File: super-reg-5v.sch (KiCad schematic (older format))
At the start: 41 parts, among them Q1 2SA1015, Q2 D44H11, U1 LM317T, U2 AD825, U3 AD825, X1 AC_IN, X2 DC_OUT

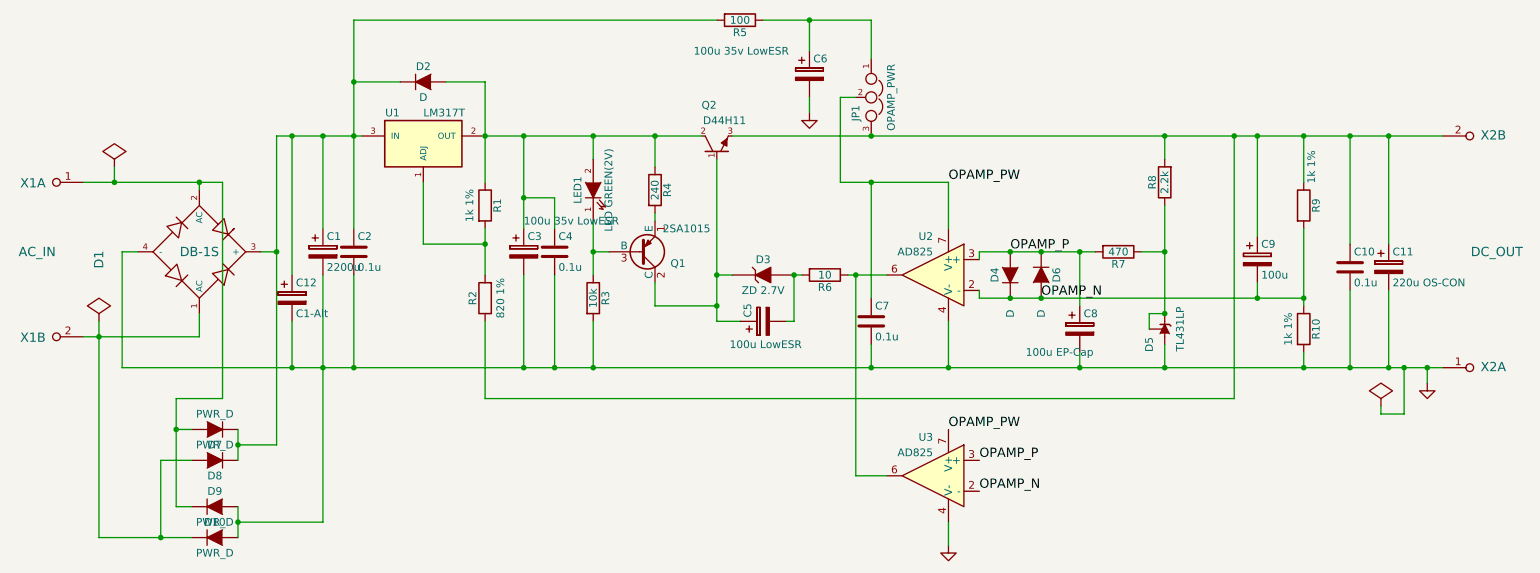
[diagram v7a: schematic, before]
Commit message: change bypass Cap
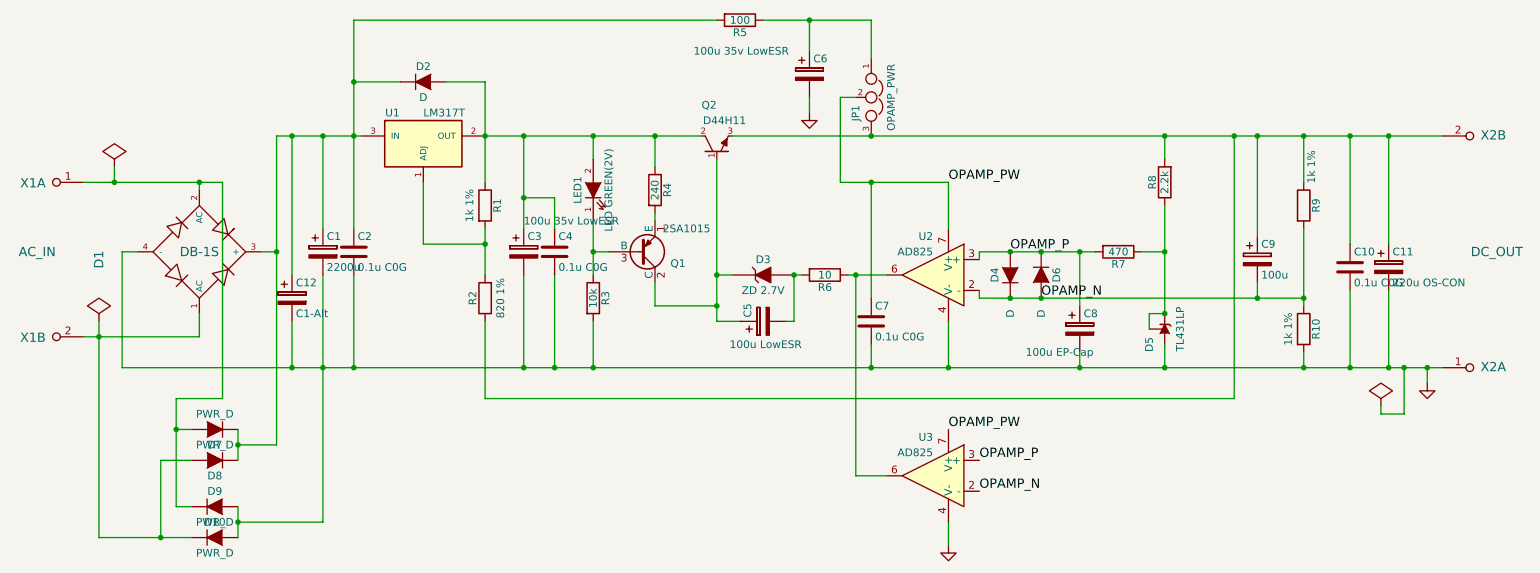
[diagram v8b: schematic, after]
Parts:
- C10, C2, C4, C7: value 0.1u -> 0.1u C0G; footprint Capacitors_SMD:C_0603_HandSoldering -> Capacitors_SMD:C_1206_HandSoldering
- R3: footprint Resistors_SMD:R_0805_HandSoldering -> Resistors_SMD:R_0603_HandSoldering
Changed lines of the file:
@@
 P 3150 3450
 F 0 "C2" H 3175 3550 50  0000 L CNN
-F 1 "0.1u" H 3175 3350 50  0000 L CNN
-F 2 "Capacitors_SMD:C_0603_HandSoldering" H 3188 3300 50  0001 C CNN
+F 1 "0.1u C0G" H 3175 3350 50  0000 L CNN
+F 2 "Capacitors_SMD:C_1206_HandSoldering" H 3188 3300 50  0001 C CNN
 F 3 "" H 3150 3450 50  0000 C CNN
 	1    3150 3450
@@
 P 4450 3450
 F 0 "C4" H 4475 3550 50  0000 L CNN
-F 1 "0.1u" H 4475 3350 50  0000 L CNN
-F 2 "Capacitors_SMD:C_0603_HandSoldering" H 4488 3300 50  0001 C CNN
+F 1 "0.1u C0G" H 4475 3350 50  0000 L CNN
+F 2 "Capacitors_SMD:C_1206_HandSoldering" H 4488 3300 50  0001 C CNN
 F 3 "" H 4450 3450 50  0000 C CNN
 	1    4450 3450
@@
 F 0 "R3" V 4780 3750 50  0000 C CNN
 F 1 "10k" V 4700 3750 50  0000 C CNN
-F 2 "Resistors_SMD:R_0805_HandSoldering" V 4630 3750 50  0001 C CNN
+F 2 "Resistors_SMD:R_0603_HandSoldering" V 4630 3750 50  0001 C CNN
 F 3 "" H 4700 3750 50  0000 C CNN
 	1    4700 3750
@@
 P 6500 3900
 F 0 "C7" H 6525 4000 50  0000 L CNN
-F 1 "0.1u" H 6525 3800 50  0000 L CNN
-F 2 "Capacitors_SMD:C_0603_HandSoldering" H 6538 3750 50  0001 C CNN
+F 1 "0.1u C0G" H 6525 3800 50  0000 L CNN
+F 2 "Capacitors_SMD:C_1206_HandSoldering" H 6538 3750 50  0001 C CNN
 F 3 "" H 6500 3900 50  0000 C CNN
 	1    6500 3900
@@
 P 9600 3550
 F 0 "C10" H 9625 3650 50  0000 L CNN
-F 1 "0.1u" H 9625 3450 50  0000 L CNN
-F 2 "Capacitors_SMD:C_0603_HandSoldering" H 9638 3400 50  0001 C CNN
+F 1 "0.1u C0G" H 9625 3450 50  0000 L CNN
+F 2 "Capacitors_SMD:C_1206_HandSoldering" H 9638 3400 50  0001 C CNN
 F 3 "" H 9600 3550 50  0000 C CNN
 	1    9600 3550
